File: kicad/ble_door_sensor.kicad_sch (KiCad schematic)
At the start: 38 parts, among them J1 Prog Header, J101 Conn_01x08, SW101 SW_Reed, SW102 SW_Push, T1 ToolingHole, T2 ToolingHole, T3 ToolingHole, U1 nRF52832-QFxx, U101 TMP100, Y1 Crystal_GND24

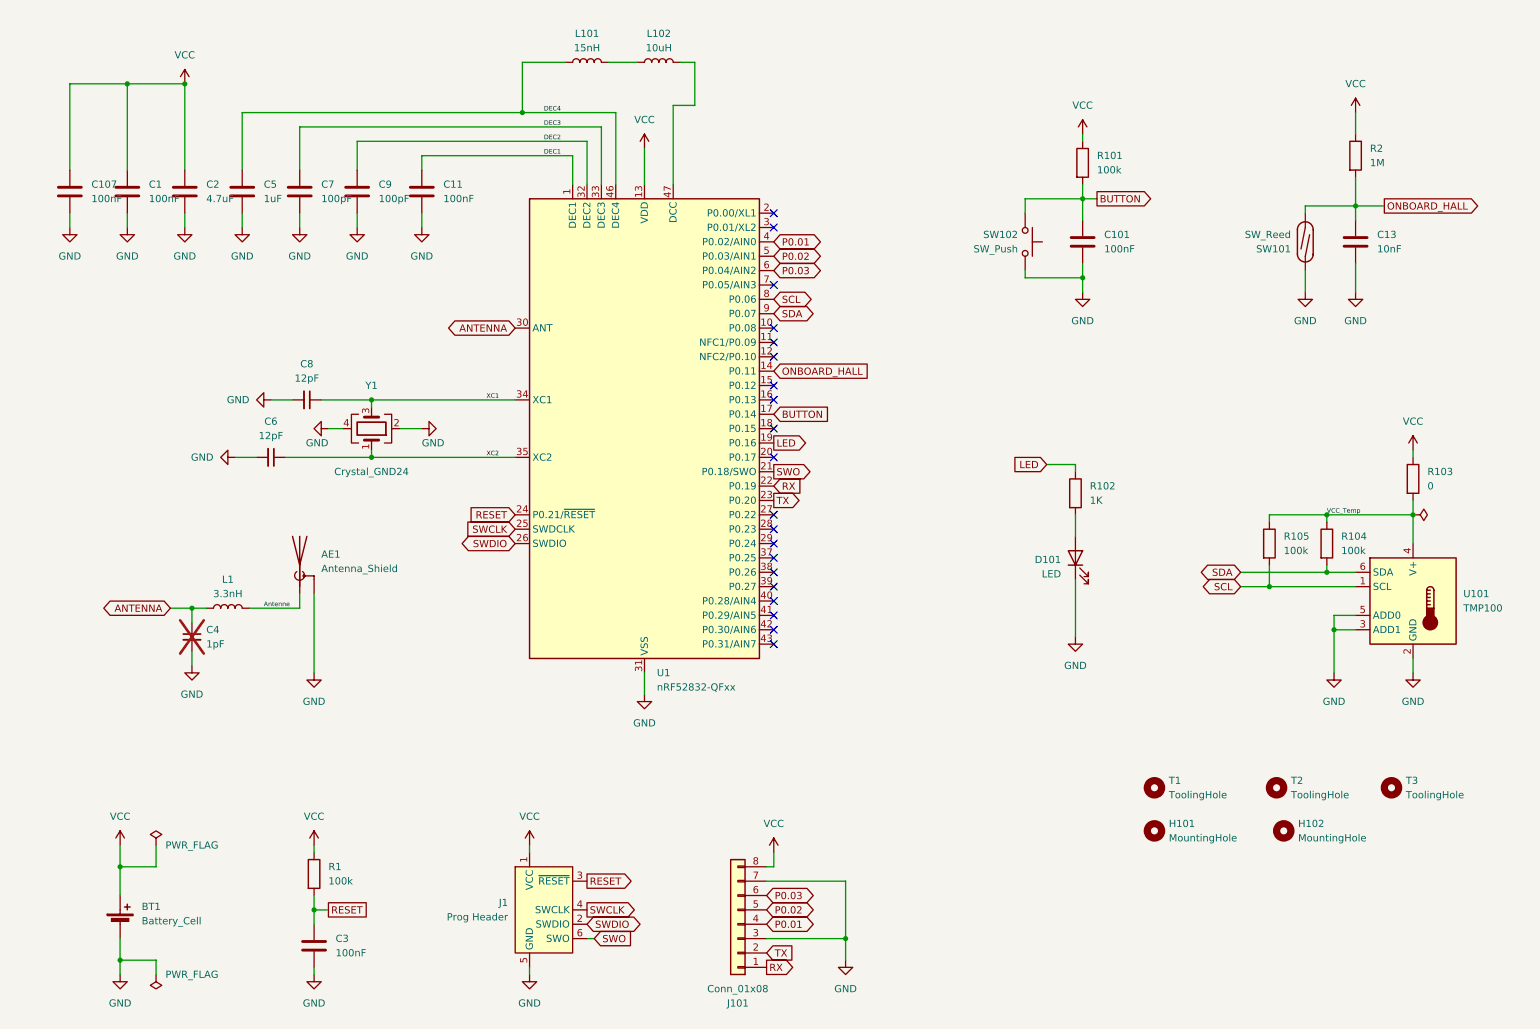
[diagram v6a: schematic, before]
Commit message: Add ambient light and humidity sensor
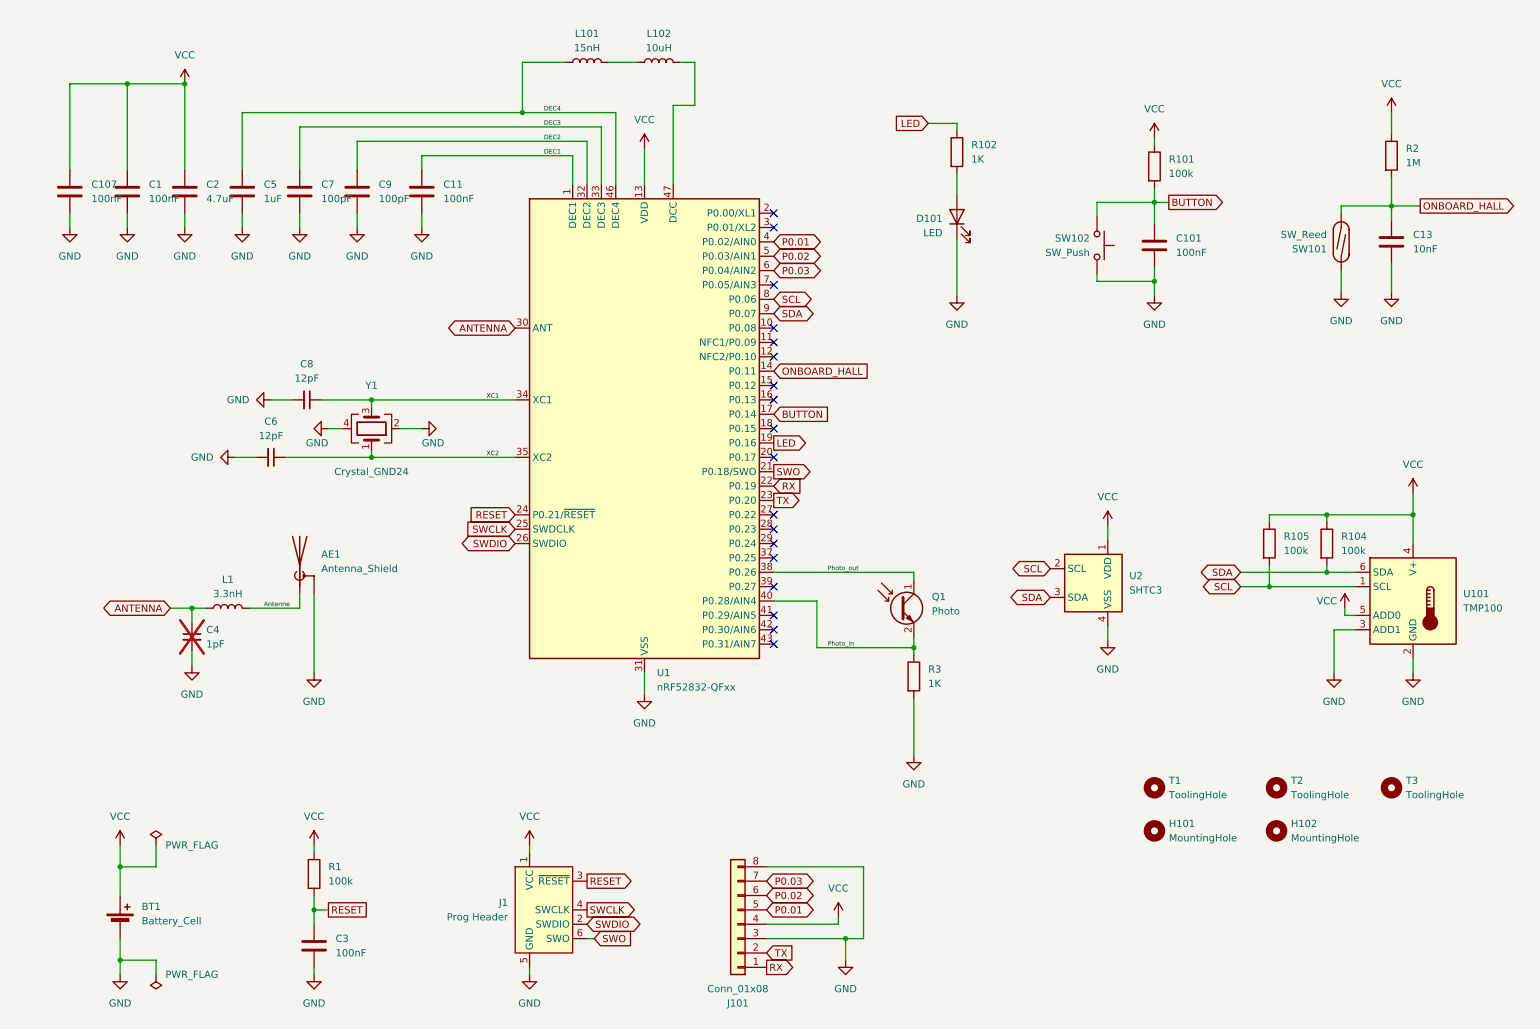
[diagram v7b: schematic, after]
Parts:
- removed R103: 0, Resistor_SMD:R_0603_1608Metric, symbol Device:R
- added Q1: Photo, LED_SMD:LED_0603_1608Metric, symbol Device:Q_Photo_NPN
- added R3: 1K, Resistor_SMD:R_0402_1005Metric, symbol Device:R
- added U2: SHTC3, Sensor_Humidity:Sensirion_DFN-4-1EP_2x2mm_P1mm_EP0.7x1.6mm, symbol Sensor_Humidity:SHTC3
- T1, T2, T3: LCSC# (none) -> -; now left out of the parts list
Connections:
- net VCC_Temp is gone; now on net VCC: R104.1, R105.1, U101.4 (V+)
- net GND: now also J101.8 (Pin_8), R3.2, U2.4 (VSS); no longer J101.7 (Pin_7), U101.5 (ADD0)
- net P0.01: now also J101.5 (Pin_5); no longer J101.4 (Pin_4)
- net P0.02: now also J101.6 (Pin_6); no longer J101.5 (Pin_5)
- net P0.03: now also J101.7 (Pin_7); no longer J101.6 (Pin_6)
- net SCL: now also U2.2 (SCL)
- net SDA: now also U2.3 (SDA)
- net VCC: now also J101.4 (Pin_4), U101.5 (ADD0), U2.1 (VDD); no longer J101.8 (Pin_8)
- net Photo_out: now reaches U1.38 (P0.26)
- net Photo_out: now also Q1.1 (C)
- net Photo_in: now reaches U1.40 (P0.28/AIN4)
- net Photo_in: now also Q1.2 (E), R3.1
- no-connect marks 20 -> 18
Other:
- moved on the sheet: C101, C13, D101, H102, R101, R102, R2, SW101, SW102
